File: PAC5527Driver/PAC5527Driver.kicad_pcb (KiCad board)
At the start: 6 copper layers, 27.5 x 27.5 mm, 77 parts, among them J1 Conn_01x08, J2 Conn_01x04, J3 Conn_01x04, J4 Conn_01x02, U1 USBLC6-2SC6, U2 SN65HVD230, U3 MA730, U4 PAC5527, U5 HT7550-1-SOT89

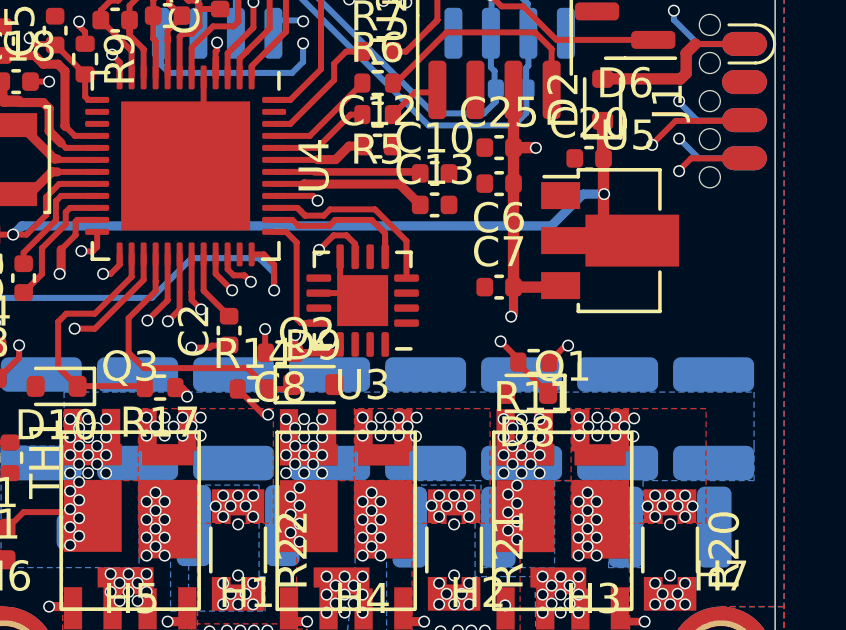
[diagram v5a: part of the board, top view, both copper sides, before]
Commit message: layout clean-up
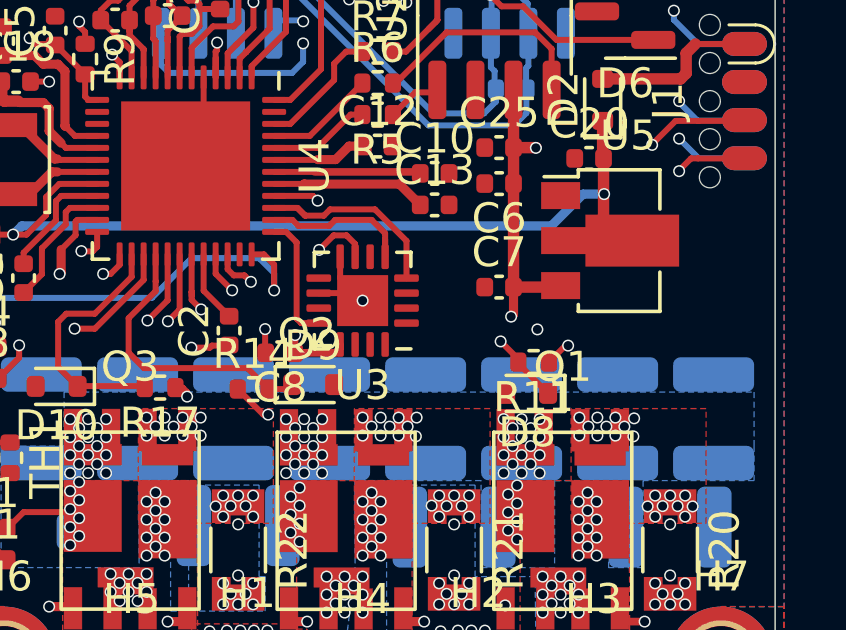
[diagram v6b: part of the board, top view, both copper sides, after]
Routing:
- net /UL: track 41.1 -> 31.2 mm
- net Net-(RN1D-R4.1): track 28.2 -> 27.7 mm
- net Net-(RN1C-R3.1): track 30.8 -> 30.2 mm
- net GND: vias 48 -> 50

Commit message: initial DRC cleanup
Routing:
- net /MB_ID_0: track 18.0 -> 22.1 mm
- net /SWDCL: track 21.9 -> 24.6 mm
- net /CAN_L: track 24.0 -> 22.4 mm
- net Net-(RN1F-R6.1): track 33.0 -> 31.6 mm
- net Net-(RN1A-R1.1): track 34.3 -> 32.9 mm
- net /SWDIO: track 20.6 -> 21.7 mm
- net VDD: track 43.9 -> 43.2 mm
- net /UART_TX: track 6.98 -> 7.67 mm
- net +3.3V: track 13.3 -> 12.7 mm, vias 3 -> 2
- net /LED_IN: track 15.5 -> 14.9 mm
- net VDC: track 28.9 -> 28.8 mm, vias 100 -> 82
- net Net-(Q2-PadSL): vias 19 -> 18
- net Net-(Q1-PadSL): vias 20 -> 18
- net GND: vias 50 -> 60
- net /WOUT: vias 34 -> 32
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
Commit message: redone layout
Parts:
- removed the C14 at (115.7, 127.4)
- removed C22, C39, C40: 10uF, Capacitor_SMD:C_1210_3225Metric
- removed D6: NUP2105L, Package_TO_SOT_SMD:SOT-23
- removed R10, R8: 10k, Resistor_SMD:R_0402_1005Metric
- removed R7: 100, Resistor_SMD:R_0402_1005Metric
- removed U5: HT7550-1-SOT89, Package_TO_SOT_SMD:SOT-89-3
- added C14: 10uF, Capacitor_SMD:C_1210_3225Metric, B.Cu at (107.1, 118.3)
- added C14: 10uF, Capacitor_SMD:C_1210_3225Metric, B.Cu at (103.2, 122.4)
- added C15: 10uF, Capacitor_SMD:C_1210_3225Metric, B.Cu at (103.2, 119.5)
- added C17: 10uF, Capacitor_SMD:C_1210_3225Metric, B.Cu at (116.0, 118.5)
- added C21: 10uF, Capacitor_SMD:C_1210_3225Metric, B.Cu at (113.0, 122.2)
- added C26: 10uF, Capacitor_SMD:C_1210_3225Metric, B.Cu at (121.2, 126.2)
- added C28: 10uF, Capacitor_SMD:C_1210_3225Metric, F.Cu at (116.7, 118.5)
- added C35: 10uF, Capacitor_SMD:C_1210_3225Metric, F.Cu at (122.5, 118.6)
- added C36: 10uF, Capacitor_SMD:C_1210_3225Metric, F.Cu at (105.3, 118.5)
- added C37: 10uF, Capacitor_SMD:C_1210_3225Metric, B.Cu at (113.0, 118.5)
- added C38: 10uF, Capacitor_SMD:C_1210_3225Metric, B.Cu at (110.0, 118.2)
- added D5: NUP2105L, Package_TO_SOT_SMD:SOT-23, F.Cu at (116.9, 103.5)
- added J5: Conn_01x06_MountingPin, Connector_JST:JST_GH_BM06B-GHS-TBT_1x06-1MP_P1.25mm_Vertical, B.Cu at (117.2, 113.2)
- added J6: Conn_01x03, Connector_PinHeader_2.54mm:PinHeader_1x03_P2.54mm_Vertical, B.Cu at (122.8, 102.9)
- added J8: Conn_01x03_MountingPin, Connector_JST:JST_GH_BM03B-GHS-TBT_1x03-1MP_P1.25mm_Vertical, B.Cu at (100.8, 111.9)
- added R2: 10k, Resistor_SMD:R_0402_1005Metric, F.Cu at (118.7, 103.6)
- added R4: 100, Resistor_SMD:R_0402_1005Metric, F.Cu at (112.5, 107.0)
- added U6: HT7533-1-SOT89, Package_TO_SOT_SMD:SOT-89-3, F.Cu at (120.9, 113.3)
- C29, C30, C31: moved to F.Cu
- H1, H2: footprint PAC5527Driver:MountingHole_SLOT_1.6_M1.5_DIN965_Pad_TopBottom -> MountingHole:MountingHole_2.2mm_M2_DIN965_Pad_TopBottom
- H3, H4, H5: footprint PAC5527Driver:MountingHole_SLOT_2.2mm_M2_DIN965_Pad_TopBottom -> MountingHole:MountingHole_2.2mm_M2_DIN965_Pad_TopOnly
- J2, J3: value Conn_01x04 -> Conn_01x04_MountingPin
- R20, R21, R22: moved to B.Cu
- R9: value 100 -> 10k
- U2: value SN65HVD230 -> TCAN330G; footprint Package_SO:SOIC-8_3.9x4.9mm_P1.27mm -> Package_TO_SOT_SMD:SOT-23-8
- moved C23 27.6 mm to (121.8, 118.5)
- moved C31 22.5 mm to (126.3, 119.3), turned to 0 degrees
- moved C27 19.7 mm to (118.8, 118.5), turned to 90 degrees
- moved R3 18.9 mm to (110.5, 115.7), turned to -90 degrees
- moved D4 17.6 mm to (109.4, 115.7), turned to -90 degrees
- moved C24 13.4 mm to (121.2, 123.4)
- moved C30 13.2 mm to (119.6, 118.5)
- moved D8 11.9 mm to (122.8, 122.2), turned to 0 degrees
- moved J1 10.4 mm to (128.2, 108.6)
- moved D9 10.4 mm to (114.2, 122.2)
- moved D10 10.3 mm to (105.5, 122.2), turned to 0 degrees
- moved R14 10.2 mm to (112.0, 122.2)
- moved H8 10.1 mm to (126.5, 103.5)
- moved Q1 9.98 mm to (121.9, 125.4), turned to -90 degrees
- moved C29 9.78 mm to (102.5, 118.5)
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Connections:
- C4 pad 1: GND -> Net-(U2-S)
- C4 pad 2: Net-(U2-Rs) -> GND
- J2 pad 1: unconnected-(J2-Pin_1-Pad1) -> GND
- J2 pad MP: (no net) -> GND
- J3 pad 1: /MB_ID_0 -> GND
- J3 pad 4: /MB_ID_1 -> unconnected-(J3-Pin_4-Pad4)
- J3 pad MP: (no net) -> GND
- U2 pad 8: Net-(U2-Rs) -> Net-(U2-S)
- U4 pad 35: unconnected-(U4D-PD5-Pad35) -> /ENC_CS1
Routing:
- net /ENC_CS1: track 0.00 -> 13.7 mm, vias 0 -> 1
- net /ENC_MISO: track 5.12 -> 18.5 mm
- net /MB_ID_0: track 22.1 -> 8.86 mm, vias 2 -> 1
- net /ENC_MOSI: track 6.65 -> 19.4 mm, vias 0 -> 1
- net Net-(U2-Rs): track 12.6 -> 0.00 mm
- net /LED_IN: track 14.9 -> 2.33 mm, vias 2 -> 0
- net /VL: track 33.2 -> 21.3 mm
- net /ENC_SCLK: track 4.23 -> 15.1 mm, vias 0 -> 1
- net /WS: track 8.51 -> 16.2 mm, vias 0 -> 2
- net /SWDCL: track 24.6 -> 31.3 mm
- net /EXT_UART_RX: track 14.9 -> 21.5 mm
- net /US: track 17.4 -> 23.7 mm
- net /PBTN: track 35.2 -> 29.1 mm
- net /VS: track 9.66 -> 15.3 mm, vias 0 -> 2
- net /EXT_UART_TX: track 19.8 -> 25.4 mm
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- added copper zone on B.Cu, net Net-(Q1-PadSL)
- added copper zone on B.Cu, net Net-(Q2-PadSL)
- added copper zone on B.Cu, net Net-(Q3-PadSL)
- added copper zone on In3.Cu, net VDC
- removed copper zone on In1.Cu, net /UOUT
- removed copper zone on In2.Cu, net /UOUT
- removed copper zone on In1.Cu, net /VOUT
- removed copper zone on In2.Cu, net /VOUT
- removed copper zone on In1.Cu, net /WOUT
- removed copper zone on In2.Cu, net /WOUT
- removed copper zone on In1.Cu, net Net-(Q1-PadSL)
- removed copper zone on In2.Cu, net Net-(Q1-PadSL)
- removed copper zone on In1.Cu, net Net-(Q2-PadSL)
- removed copper zone on In2.Cu, net Net-(Q2-PadSL)
- removed copper zone on In1.Cu, net Net-(Q3-PadSL)
- removed copper zone on In2.Cu, net Net-(Q3-PadSL)
- removed copper zone on In4.Cu, net VDC
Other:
- board size 27.5 x 27.5 mm -> 30.5 x 30.5 mm
